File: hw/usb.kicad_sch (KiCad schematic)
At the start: 3 parts

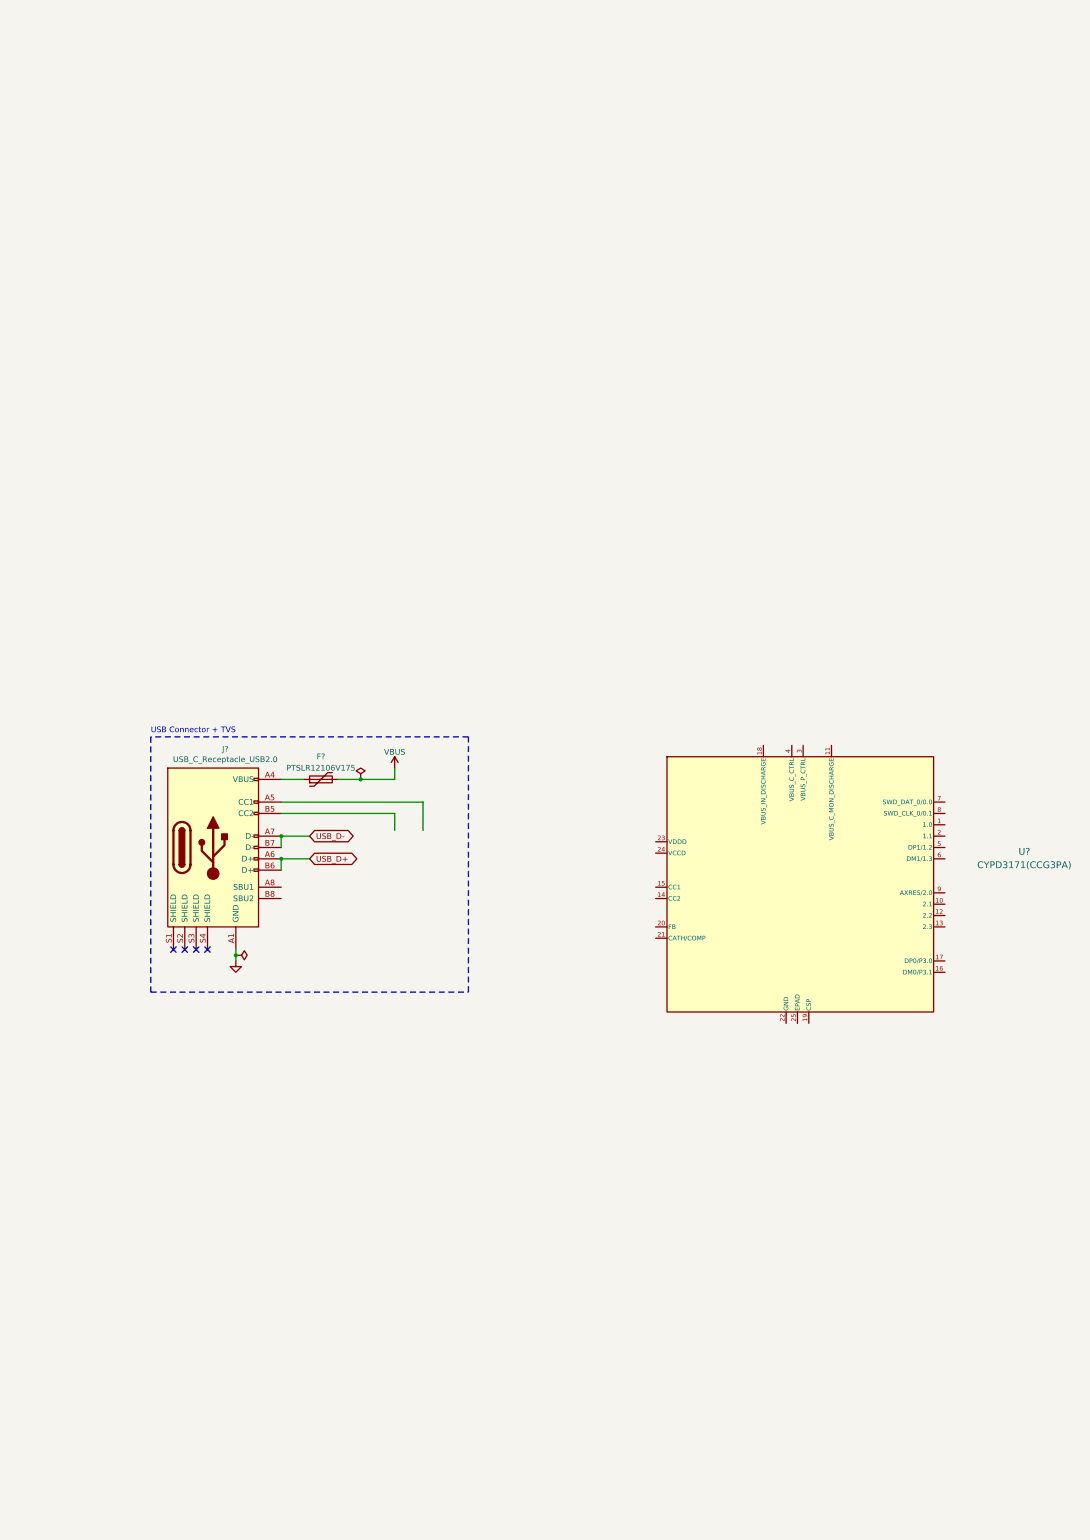
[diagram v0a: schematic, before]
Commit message: Messed up system layout, consumer from receptacle, datasheet uses left to right
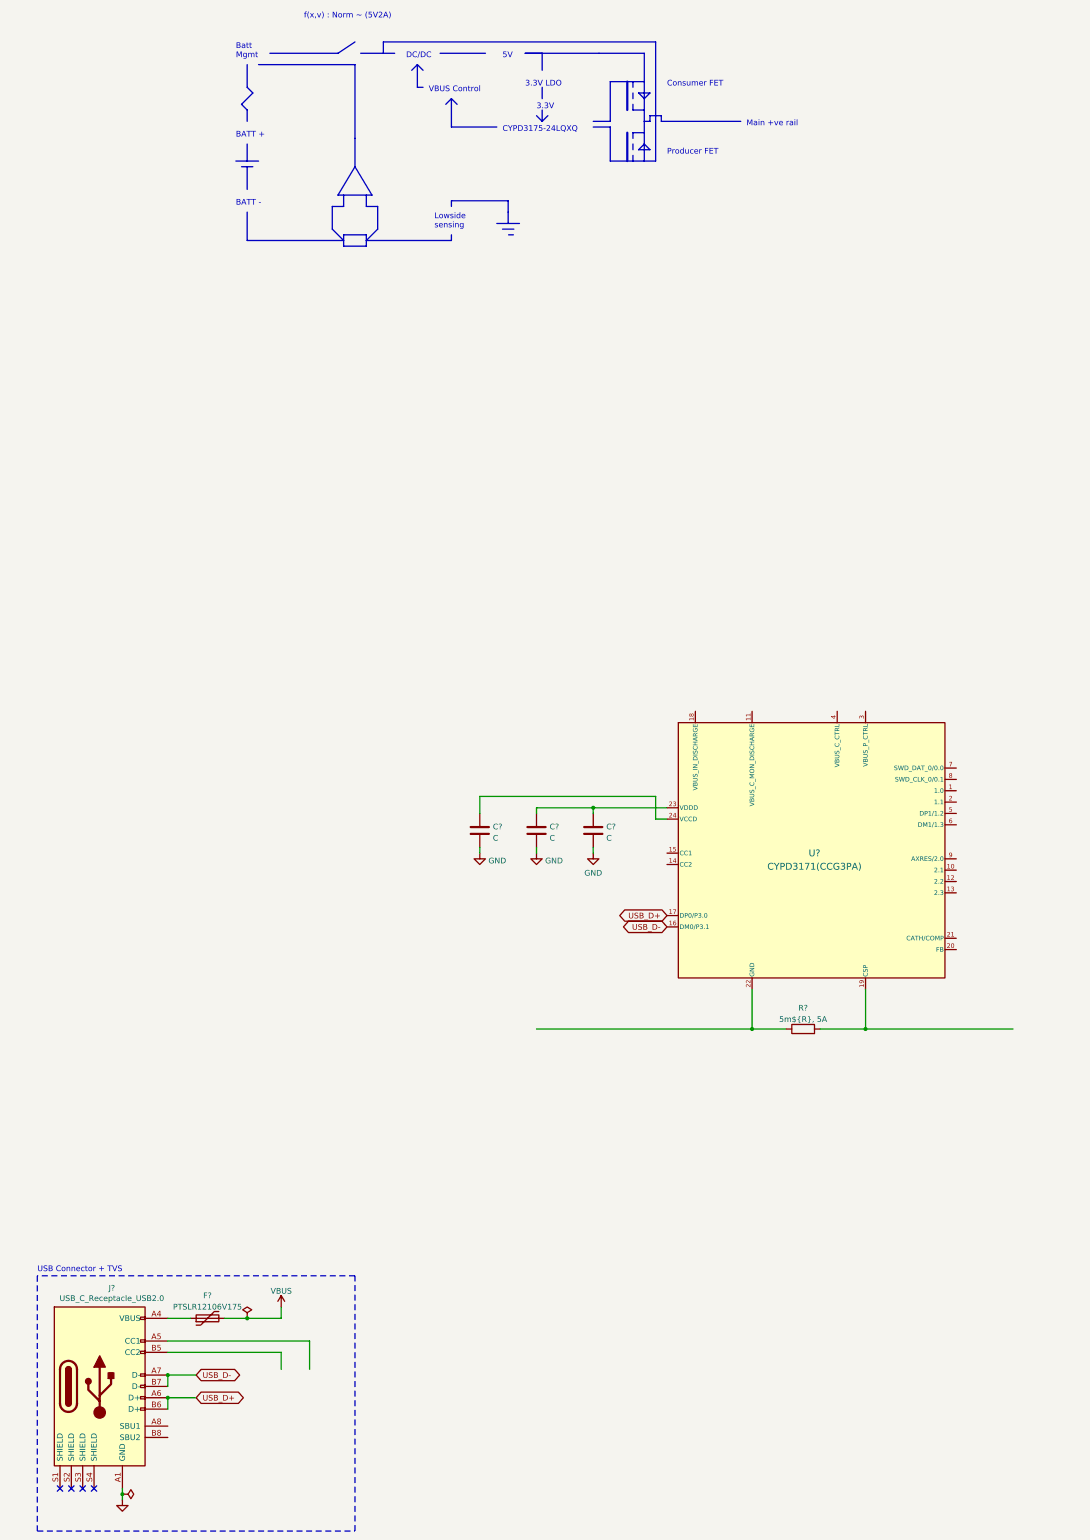
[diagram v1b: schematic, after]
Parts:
- added C? (x3): C, symbol Device:C
- added R?: 5m${R}, 5A, symbol Device:R
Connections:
- net GND: now also C?.2, C?.2, C?.2
- net USB_D+: now also U?.17 (DP0/P3.0)
- net USB_D-: now also U?.16 (DM0/P3.1)
- net at U?.19 (CSP): now also R?.2
- net at U?.22 (GND): now also U?.25 (EPAD), R?.1
- net at U?.23 (VDDD): now also C?.1, C?.1
- net at U?.24 (VCCD): now also C?.1
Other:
- note added: "3.3V"
- note added: "3.3V LDO"
- note added: "5V"
- note added: "BATT +"
- note added: "BATT -"
- note added: "Batt Mgmt"
- note added: "CYPD3175-24LQXQ"
- note added: "Consumer FET"
- note added: "DC/DC"
- note added: "Lowside sensing"
- note added: "Main +ve rail"
- note added: "Producer FET"
- note added: "VBUS Control"
- note added: "f(x,v) : Norm ~ (5V2A)"
- moved on the sheet: F?, J?

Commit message: System sketch
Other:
- note added: "CC[1:2]"
- note added: "DP0, DM0"
- note added: "Polyfuse"
- note added: "VBUS"
- note added: "VBUS_IN_DISCHARGE"
- note added: "VDDD"
- note removed: "Main +ve rail"

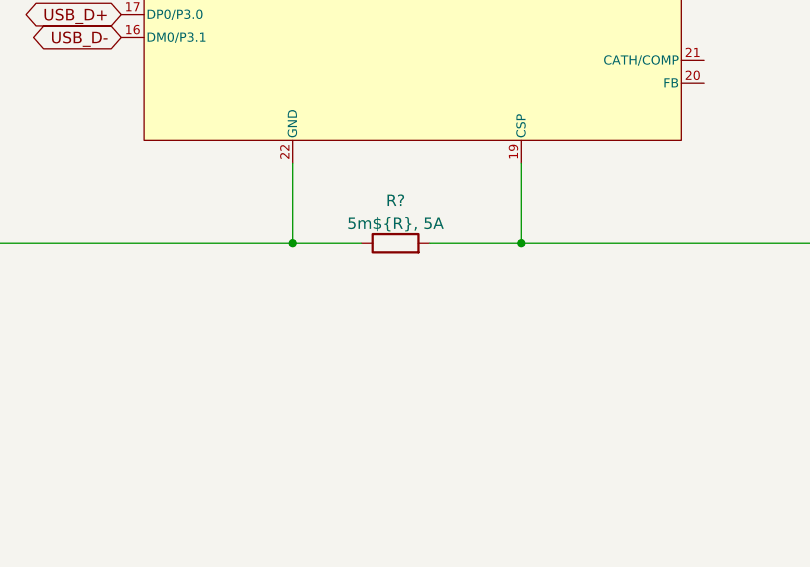
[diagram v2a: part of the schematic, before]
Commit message: MAX77751CEFG+ Symbol fix
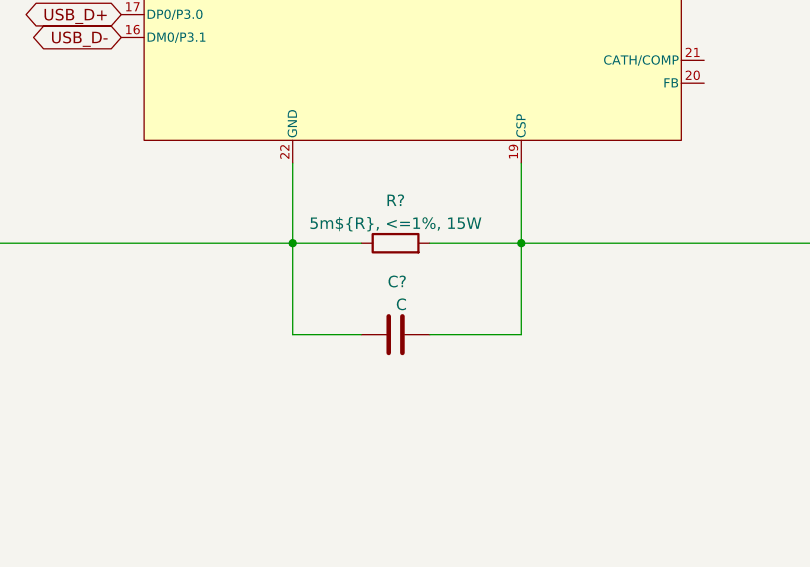
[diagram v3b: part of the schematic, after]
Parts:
- added C?: C, symbol Device:C
- R?: value 5m${R}, 5A -> 5m${R}, <=1%, 15W
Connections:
- net at R?.1, U?.22 (GND), U?.25 (EPAD): now also C?.1
- net at R?.2, U?.19 (CSP): now also C?.2
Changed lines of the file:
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@@
     (stroke (width 0) (type solid) (color 0 0 0 0))
+  )
+  (wire (pts (xy 176.53 97.79) (xy 168.91 97.79))
+    (stroke (width 0) (type default) (color 0 0 0 0))
   )
   (polyline (pts (xy 72.39 -22.86) (xy 72.39 -16.51))
@@
     (stroke (width 0) (type default) (color 0 0 0 0))
   )
+  (wire (pts (xy 194.31 97.79) (xy 194.31 87.63))
+    (stroke (width 0) (type default) (color 0 0 0 0))
+  )
   (wire (pts (xy 184.15 87.63) (xy 194.31 87.63))
     (stroke (width 0) (type default) (color 0 0 0 0))
@@
   (polyline (pts (xy 67.31 -50.8) (xy 83.82 -50.8))
     (stroke (width 0) (type solid) (color 0 0 0 0))
+  )
+  (wire (pts (xy 184.15 97.79) (xy 194.31 97.79))
+    (stroke (width 0) (type default) (color 0 0 0 0))
   )
   (polyline (pts (xy 95.25 -36.83) (xy 97.79 -36.83))
@@
   (polyline (pts (xy 90.17 -33.02) (xy 90.17 -26.67))
     (stroke (width 0.5) (type solid) (color 0 0 0 0))
+  )
+  (wire (pts (xy 168.91 87.63) (xy 168.91 97.79))
+    (stroke (width 0) (type default) (color 0 0 0 0))
   )
   (polyline (pts (xy 5.08 -15.24) (xy 5.08 -8.89))
@@
     (pin "1")
   )
+  (symbol (lib_id "Device:C") (at 180.34 97.79 90) (unit 1)
+    (in_bom yes) (on_board yes) (fields_autoplaced)
+    (property "Reference" "C?" (id 0) (at 181.5987 91.9312 90)
+      (effects (font (size 1.27 1.27)) (justify left))
+    )
+    (property "Value" "C" (id 1) (at 181.5987 94.4681 90)
+      (effects (font (size 1.27 1.27)) (justify left))
+    )
+    (property "Footprint" "" (id 2) (at 184.15 96.8248 0)
+      (effects (font (size 1.27 1.27)) hide)
+    )
+    (property "Datasheet" "~" (id 3) (at 180.34 97.79 0)
+      (effects (font (size 1.27 1.27)) hide)
+    )
+    (pin "1")
+    (pin "2")
+  )
   (symbol (lib_id "1.Fuses:PTSLR12106V175") (at 46.99 152.4 90) (unit 1)
     (in_bom yes) (on_board yes) (fields_autoplaced)
@@
     (in_bom yes) (on_board yes) (fields_autoplaced)
     (property "Reference" "R?" (id 0) (at 180.34 82.9142 90))
-    (property "Value" "5m${R}, 5A" (id 1) (at 180.34 85.4511 90))
+    (property "Value" "5m${R}, <=1%, 15W" (id 1) (at 180.34 85.4511 90))
     (property "Footprint" "" (id 2) (at 180.34 89.408 90)
       (effects (font (size 1.27 1.27)) hide)

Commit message: lolz
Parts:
- removed C? (x4): C, symbol Device:C
- removed F?: PTSLR12106V175, Fuse:Fuse_1210_3225Metric, symbol 1.Fuses:PTSLR12106V175
- removed J?: USB_C_Receptacle_USB2.0, footprints:USB-C_C168688, symbol mikoto:USB_C_Receptacle_USB2.0
- removed R?: 5m${R}, <=1%, 15W, symbol Device:R
- removed U?: CYPD3171(CCG3PA), 1.Embedded.Specialized:CYPD3171-24LQXQ, symbol 1.Embedded.Specialized:CYPD3171(CCG3PA)
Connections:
- no-connect marks 4 -> 0
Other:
- note removed: "3.3V"
- note removed: "3.3V LDO"
- note removed: "5V"
- note removed: "BATT +"
- note removed: "BATT -"
- note removed: "Batt Mgmt"
- note removed: "CC[1:2]"
- note removed: "CYPD3175-24LQXQ"
- note removed: "Consumer FET"
- note removed: "DC/DC"
- note removed: "DP0, DM0"
- note removed: "Lowside sensing"
- note removed: "Polyfuse"
- note removed: "Producer FET"
- note removed: "USB Connector + TVS"
- note removed: "VBUS"
- note removed: "VBUS Control"
- note removed: "VBUS_IN_DISCHARGE"
- note removed: "VDDD"
- note removed: "f(x,v) : Norm ~ (5V2A)"
